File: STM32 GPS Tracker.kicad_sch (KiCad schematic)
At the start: 57 parts, among them J1 Screw_Terminal_01x02, J2 Conn_01x08_Pin, J3 693010020611, J4 Conn_01x08_Pin, Q1 AO3407A, SW1 SW_Push, SW2 SW_Push, U1 SIM808, U2 TPS5430DDA, U3 SMF05CT1G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

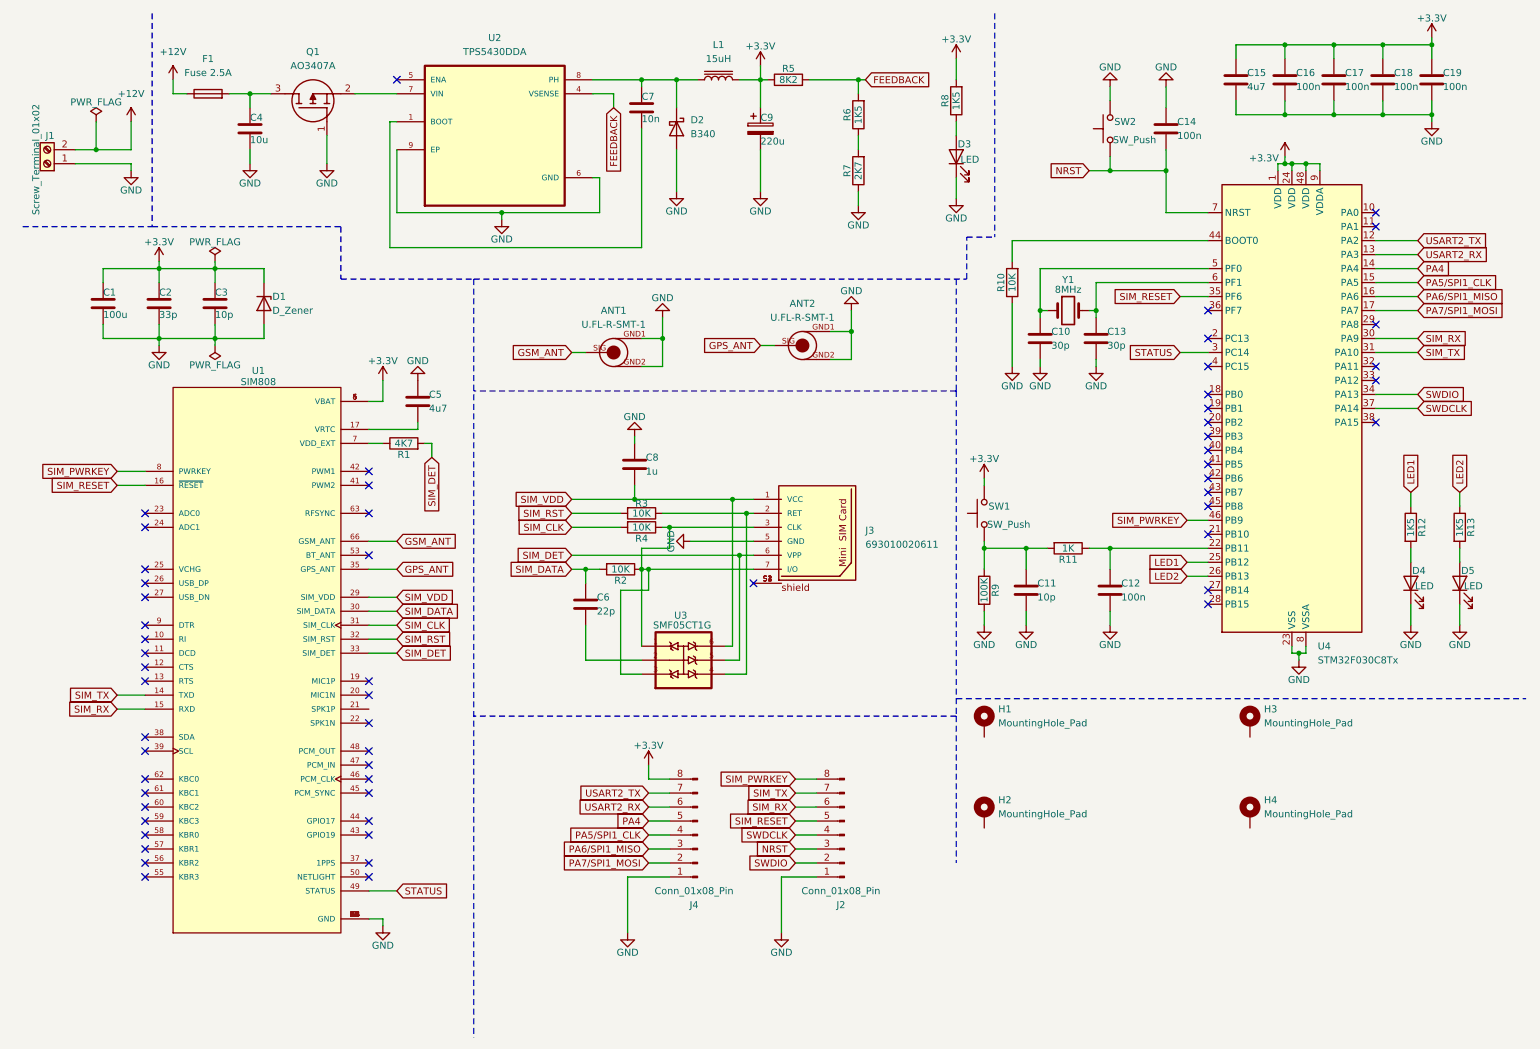
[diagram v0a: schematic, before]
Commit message: Placed the Texts in Schematic
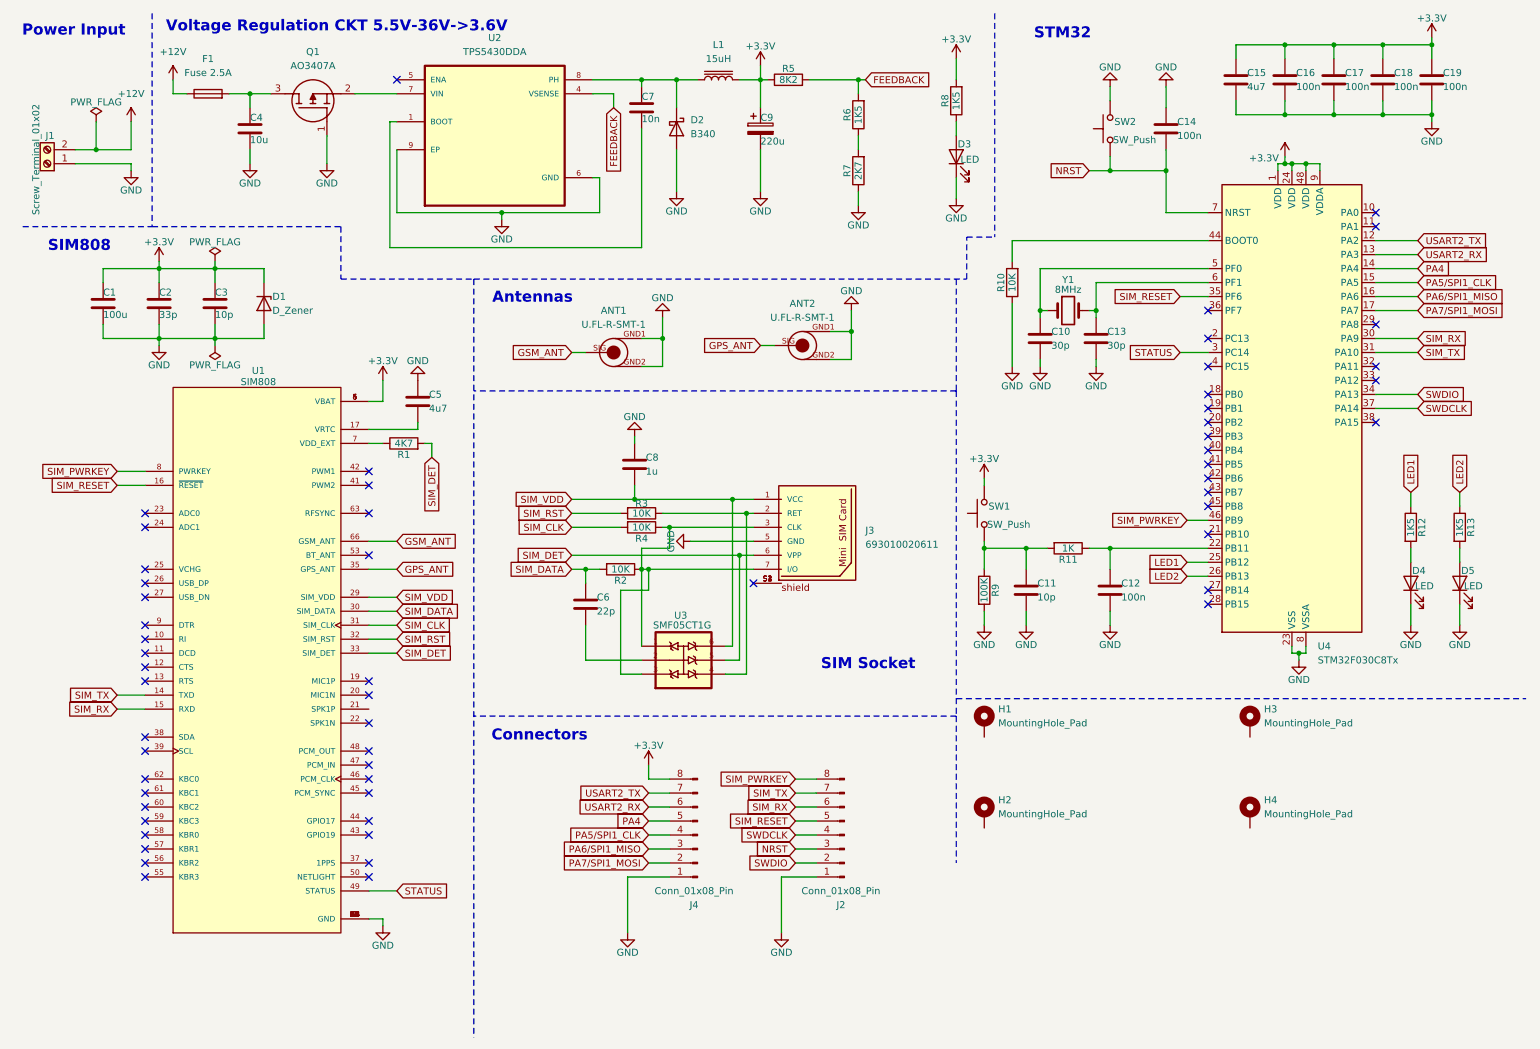
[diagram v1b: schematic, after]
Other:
- note added: "Antennas"
- note added: "Connectors"
- note added: "Power Input"
- note added: "SIM Socket"
- note added: "SIM808"
- note added: "STM32"
- note added: "Voltage Regulation CKT 5.5V-36V->3.6V"
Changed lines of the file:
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@@
 	(generator_version "9.0")
 	(paper "A4")
+	(text "Voltage Regulation CKT 5.5V-36V->3.6V"
+		(exclude_from_sim no)
+		(at 69.088 14.478 0)
+		(effects
+			(font
+				(face "KiCad Font")
+				(size 2 2)
+				(thickness 0.254)
+				(bold yes)
+			)
+		)
+	)
+	(text "Connectors"
+		(exclude_from_sim no)
+		(at 105.918 143.256 0)
+		(effects
+			(font
+				(face "KiCad Font")
+				(size 2 2)
+				(thickness 0.254)
+				(bold yes)
+			)
+		)
+	)
+	(text "STM32"
+		(exclude_from_sim no)
+		(at 200.914 15.748 0)
+		(effects
+			(font
+				(face "KiCad Font")
+				(size 2 2)
+				(thickness 0.254)
+				(bold yes)
+			)
+		)
+	)
+	(text "SIM Socket"
+		(exclude_from_sim no)
+		(at 165.608 130.302 0)
+		(effects
+			(font
+				(face "KiCad Font")
+				(size 2 2)
+				(thickness 0.254)
+				(bold yes)
+			)
+		)
+	)
+	(text "Power Input"
+		(exclude_from_sim no)
+		(at 21.336 15.24 0)
+		(effects
+			(font
+				(face "KiCad Font")
+				(size 2 2)
+				(thickness 0.254)
+				(bold yes)
+			)
+		)
+	)
+	(text "SIM808"
+		(exclude_from_sim no)
+		(at 22.352 54.356 0)
+		(effects
+			(font
+				(face "KiCad Font")
+				(size 2 2)
+				(thickness 0.254)
+				(bold yes)
+			)
+		)
+	)
+	(text "Antennas"
+		(exclude_from_sim no)
+		(at 104.648 63.754 0)
+		(effects
+			(font
+				(face "KiCad Font")
+				(size 2 2)
+				(thickness 0.254)
+				(bold yes)
+			)
+		)
+	)
 	(junction
 		(at 129.54 105.41)

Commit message: Assigned the Footprints
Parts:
- C1: footprint (none) -> Capacitor_SMD:C_1206_3216Metric
- C10, C11, C12, C13, C14, C16, C17, C18, C19, C2, C3, C6, C8: footprint (none) -> Capacitor_SMD:C_0402_1005Metric
- C15, C5, C7: footprint (none) -> Capacitor_SMD:C_0201_0603Metric
- C4: footprint (none) -> Capacitor_SMD:C_0805_2012Metric
- C9: footprint (none) -> Capacitor_Tantalum_SMD:CP_EIA-7343-15_Kemet-W
- D1: footprint (none) -> Diode_SMD:D_0805_2012Metric
- D3, D4, D5: footprint (none) -> LED_SMD:LED_0201_0603Metric
- F1: footprint (none) -> Fuse:Fuse_0402_1005Metric
- GPS1: renamed from ANT2; footprint U.FL-R-SMT-1:U.FL-R-SMT-1 -> Footprints:U.FL-R-SMT-1
- GSM1: renamed from ANT1; footprint U.FL-R-SMT-1:U.FL-R-SMT-1 -> Footprints:U.FL-R-SMT-1
- H1, H2, H3, H4: footprint (none) -> MountingHole:MountingHole_2.2mm_M2_Pad_Via
- J1: footprint (none) -> TerminalBlock:TerminalBlock_bornier-2_P5.08mm
- J2: renamed from J4; value Conn_01x08_Pin -> LEFT HEADER PINS; footprint (none) -> Connector_PinHeader_2.54mm:PinHeader_1x08_P2.54mm_Vertical
- J3: footprint 693010020611:693010020611 -> Footprints:693010020611
- J4: renamed from J2; value Conn_01x08_Pin -> RIGHT HEADER PINS; footprint (none) -> Connector_PinHeader_2.54mm:PinHeader_1x08_P2.54mm_Vertical
- L1: footprint (none) -> Inductor_SMD:L_10.4x10.4_H4.8
- Q1: footprint SOT95P280X125-3N -> Footprints:SOT95P280X125-3N
- R1, R10, R2, R3, R4: footprint (none) -> Resistor_SMD:R_0402_1005Metric
- R11: footprint (none) -> Resistor_SMD:R_0603_1608Metric
- R12, R13, R5, R6, R7, R8: footprint (none) -> Resistor_SMD:R_0805_2012Metric
- R9: footprint (none) -> Resistor_SMD:R_0201_0603Metric
- SW1, SW2: footprint (none) -> Button_Switch_SMD:SW_Push_1P1T_NO_CK_KSC6xxJ
- U1: footprint SIM808:XCVR_SIM808 -> Footprints:XCVR_SIM808
- U2: footprint TPS5430DDA:VREG_LM5017MR_NOPB -> Footprints:VREG_LM5017MR_NOPB
- U3: footprint SMF05CT1G:SOT65P210X110-6N -> Footprints:SOT65P210X110-6N
- Y1: footprint (none) -> Crystal:Crystal_SMD_5032-2Pin_5.0x3.2mm
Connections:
- net GND: now also H1.1, H2.1, H3.1, H4.1
- no-connect marks 58 -> 59

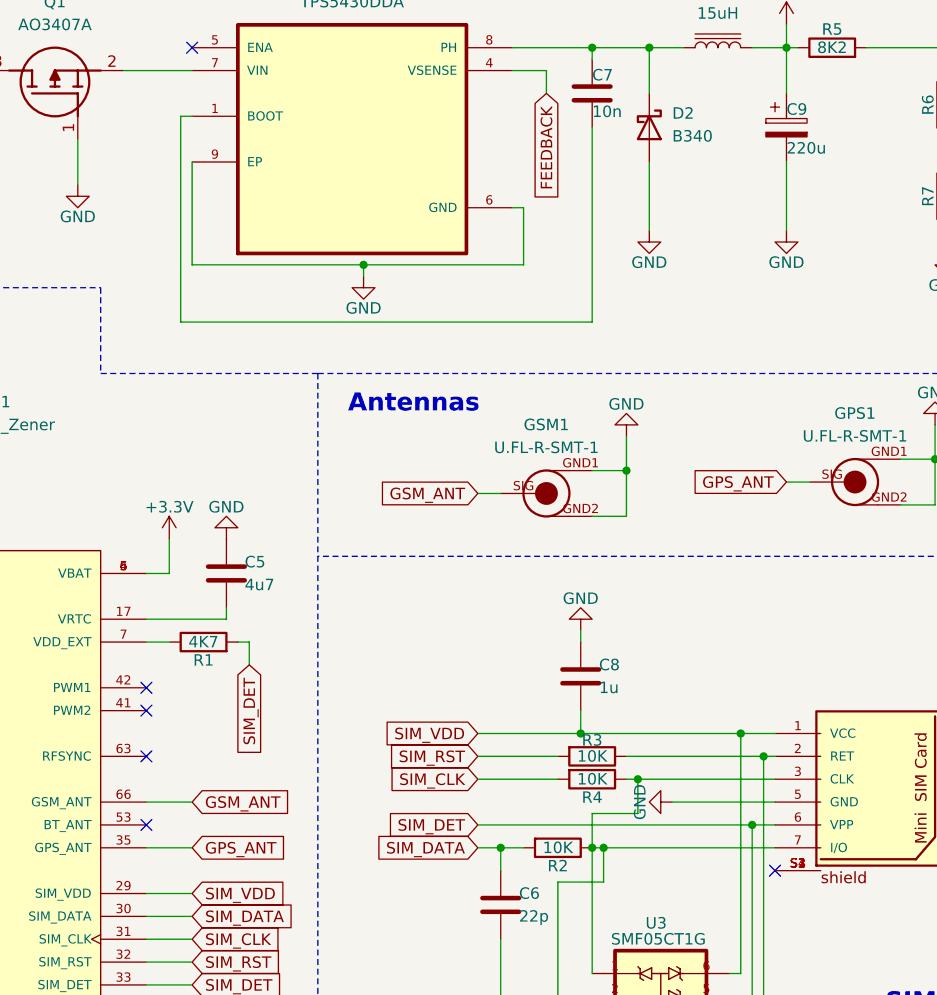
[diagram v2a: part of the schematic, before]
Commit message: Add STM32F0 GPS tracker firmware (Phase 1-3)
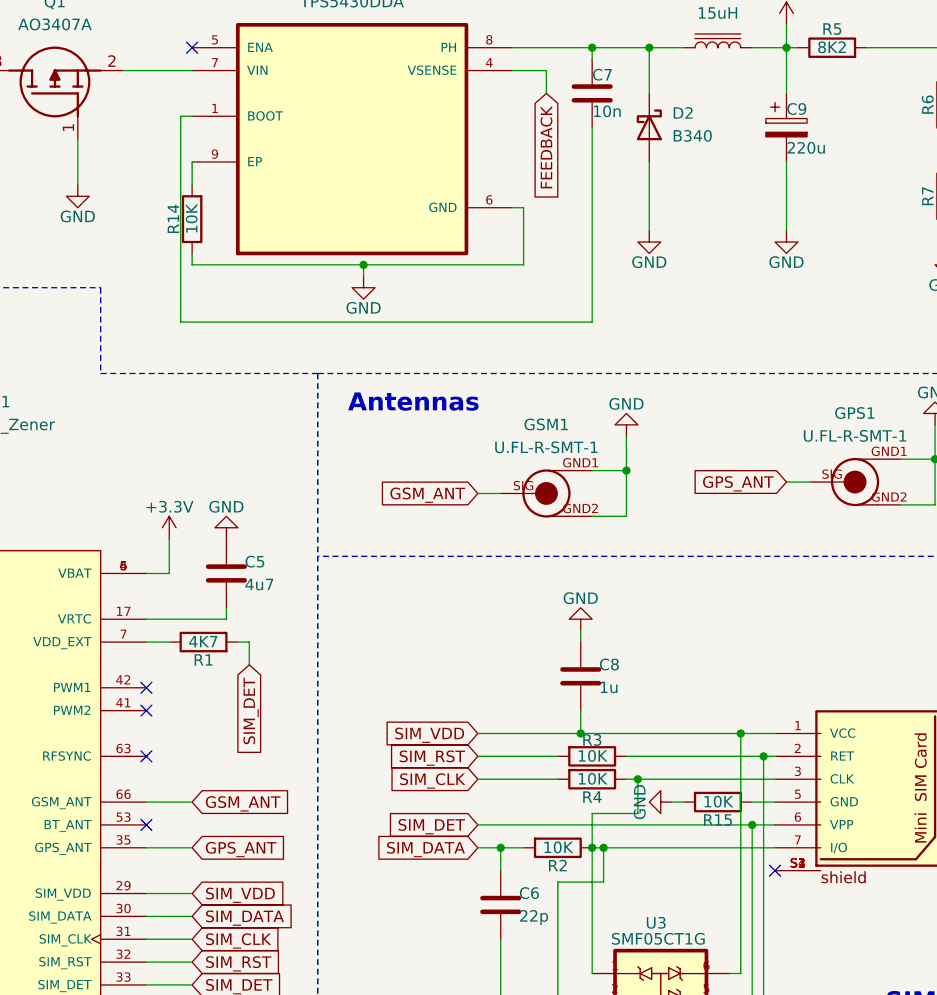
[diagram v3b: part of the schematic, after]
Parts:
- added R14, R15: 10K, Resistor_SMD:R_0402_1005Metric, symbol Device:R
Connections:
- net GND: now also R14.1, R15.2; no longer J3.5 (GND), U2.9 (EP)
- new net: R14.2, U2.9 (EP)
- new net: J3.5 (GND), R15.1
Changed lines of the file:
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@@
 	(wire
 		(pts
+			(xy 133.35 107.95) (xy 134.62 107.95)
+		)
+		(stroke
+			(width 0)
+			(type default)
+		)
+	)
+	(wire
+		(pts
 			(xy 205.74 40.64) (xy 209.55 40.64)
 		)
@@
 	(wire
 		(pts
-			(xy 80.01 36.83) (xy 80.01 48.26)
+			(xy 80.01 36.83) (xy 80.01 39.37)
 		)
 		(stroke
@@
 	(wire
 		(pts
-			(xy 133.35 107.95) (xy 144.78 107.95)
-		)
-		(stroke
-			(width 0)
-			(type default)
-		)
-	)
-	(wire
-		(pts
 			(xy 67.31 34.29) (xy 67.31 39.37)
 		)
@@
 	(wire
 		(pts
+			(xy 142.24 107.95) (xy 144.78 107.95)
+		)
+		(stroke
+			(width 0)
+			(type default)
+		)
+	)
+	(wire
+		(pts
 			(xy 142.24 129.54) (xy 142.24 110.49)
 		)
@@
 	(wire
 		(pts
+			(xy 80.01 46.99) (xy 80.01 48.26)
+		)
+		(stroke
+			(width 0)
+			(type default)
+		)
+	)
+	(wire
+		(pts
 			(xy 152.4 163.83) (xy 156.21 163.83)
 		)
@@
 	)
 	(symbol
+		(lib_id "Device:R")
+		(at 138.43 107.95 270)
+		(unit 1)
+		(exclude_from_sim no)
+		(in_bom yes)
+		(on_board yes)
+		(dnp no)
+		(property "Reference" "R15"
+			(at 138.43 109.982 90)
+			(effects
+				(font
+					(size 1.27 1.27)
+				)
+			)
+		)
+		(property "Value" "10K"
+			(at 138.43 107.95 90)
+			(effects
+				(font
+					(size 1.27 1.27)
+				)
+			)
+		)
+		(property "Footprint" "Resistor_SMD:R_0402_1005Metric"
+			(at 138.43 106.172 90)
+			(effects
+				(font
+					(size 1.27 1.27)
+				)
+				(hide yes)
+			)
+		)
+		(property "Datasheet" "~"
+			(at 138.43 107.95 0)
+			(effects
+				(font
+					(size 1.27 1.27)
+				)
+				(hide yes)
+			)
+		)
+		(property "Description" "Resistor"
+			(at 138.43 107.95 0)
+			(effects
+				(font
+					(size 1.27 1.27)
+				)
+				(hide yes)
+			)
+		)
+		(pin "1"
+		)
+		(pin "2"
+		)
+		(instances
+			(project "STM32 GPS Tracker"
+				(path "/320039b8-7fce-4c2b-9942-11f4784b13b1"
+					(reference "R15")
+					(unit 1)
+				)
+			)
+		)
+	)
+	(symbol
+		(lib_id "Device:R")
+		(at 80.01 43.18 180)
+		(unit 1)
+		(exclude_from_sim no)
+		(in_bom yes)
+		(on_board yes)
+		(dnp no)
+		(property "Reference" "R14"
+			(at 77.978 43.18 90)
+			(effects
+				(font
+					(size 1.27 1.27)
+				)
+			)
+		)
+		(property "Value" "10K"
+			(at 80.01 43.18 90)
+			(effects
+				(font
+					(size 1.27 1.27)
+				)
+			)
+		)
+		(property "Footprint" "Resistor_SMD:R_0402_1005Metric"
+			(at 81.788 43.18 90)
+			(effects
+				(font
+					(size 1.27 1.27)
+				)
+				(hide yes)
+			)
+		)
+		(property "Datasheet" "~"
+			(at 80.01 43.18 0)
+			(effects
+				(font
+					(size 1.27 1.27)
+				)
+				(hide yes)
+			)
+		)
+		(property "Description" "Resistor"
+			(at 80.01 43.18 0)
+			(effects
+				(font
+					(size 1.27 1.27)
+				)
+				(hide yes)
+			)
+		)
+		(pin "1"
+		)
+		(pin "2"
+		)
+		(instances
+			(project "STM32 GPS Tracker"
+				(path "/320039b8-7fce-4c2b-9942-11f4784b13b1"
+					(reference "R14")
+					(unit 1)
+				)
+			)
+		)
+	)
+	(symbol
 		(lib_id "power:GND")
 		(at 219.71 25.4 180)
@@
 	)
 	(symbol
+		(lib_name "U.FL-R-SMT-1_1")
 		(lib_id "U.FL-R-SMT-1:U.FL-R-SMT-1")
 		(at 119.38 73.66 0)
